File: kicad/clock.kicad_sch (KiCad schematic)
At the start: 15 parts, among them Q2 BC547, SW1 Reset, U18 NE555P, U19 74HC163, X1 25.175 MHz

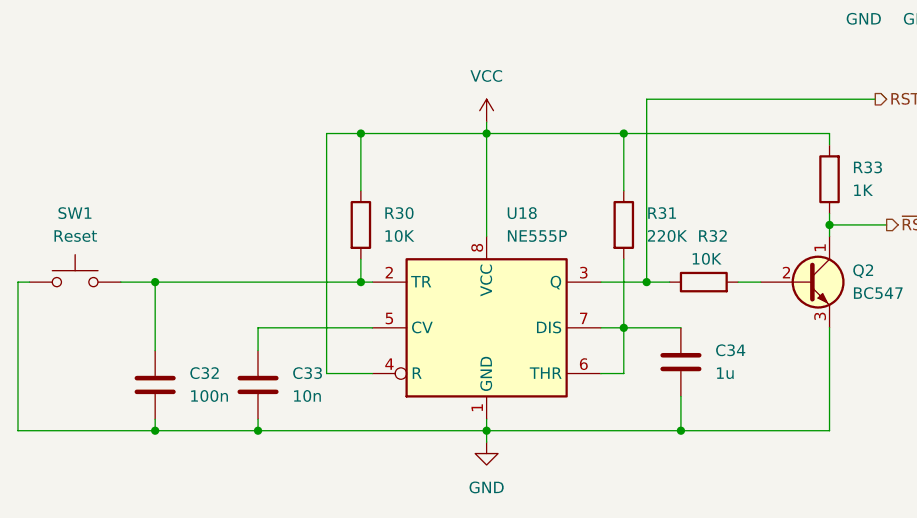
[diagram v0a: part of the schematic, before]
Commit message: HW: Fix unconnected /SOUND net, add /RST header and /DTR power supply
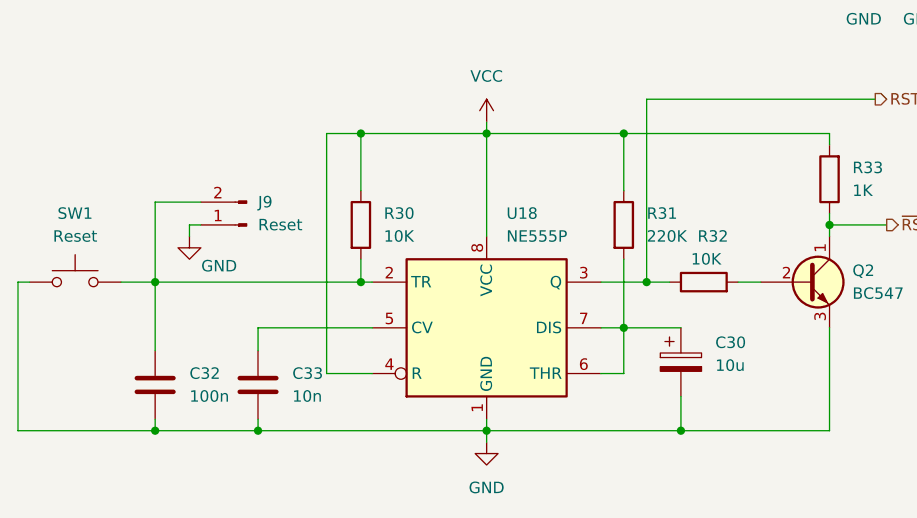
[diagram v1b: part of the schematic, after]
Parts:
- removed C34: 1u, Capacitor_THT:C_Disc_D5.0mm_W2.5mm_P2.50mm, symbol Device:C
- added C30: 10u, Capacitor_THT:CP_Radial_D5.0mm_P2.50mm, symbol Device:C_Polarized
- added J9: Reset, Connector_PinHeader_2.54mm:PinHeader_1x02_P2.54mm_Vertical, symbol Connector:Conn_01x02_Pin
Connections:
- net GND: now also C30.2, J9.1 (Pin_1)
- net at R31.2, U18.6 (THR), U18.7 (DIS): now also C30.1
- net at C32.1, R30.2, SW1.2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: now also J9.2 (Pin_2)
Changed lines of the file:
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@@
+	(wire
+		(pts
+			(xy 101.6 118.11) (xy 102.87 118.11)
+		)
+		(stroke
+			(width 0)
+			(type default)
+		)
+	)
 	(wire
 		(pts
@@
 	(wire
 		(pts
+			(xy 102.87 115.57) (xy 97.79 115.57)
+		)
+		(stroke
+			(width 0)
+			(type default)
+		)
+	)
+	(wire
+		(pts
 			(xy 139.7 40.64) (xy 139.7 49.53)
 		)
@@
 	(wire
 		(pts
+			(xy 101.6 119.38) (xy 101.6 118.11)
+		)
+		(stroke
+			(width 0)
+			(type default)
+		)
+	)
+	(wire
+		(pts
 			(xy 172.72 107.95) (xy 172.72 109.22)
 		)
@@
 		(pts
 			(xy 134.62 142.24) (xy 134.62 140.97)
+		)
+		(stroke
+			(width 0)
+			(type default)
+		)
+	)
+	(wire
+		(pts
+			(xy 97.79 115.57) (xy 97.79 124.46)
 		)
 		(stroke
@@
 	)
 	(symbol
-		(lib_id "Device:C")
-		(at 156.21 133.35 0)
-		(unit 1)
-		(exclude_from_sim no)
-		(in_bom yes)
-		(on_board yes)
-		(dnp no)
-		(fields_autoplaced yes)
-		(property "Reference" "C34"
-			(at 160.02 132.0799 0)
-			(effects
-				(font
-					(size 1.27 1.27)
-				)
-				(justify left)
-			)
-		)
-		(property "Value" "1u"
-			(at 160.02 134.6199 0)
-			(effects
-				(font
-					(size 1.27 1.27)
-				)
-				(justify left)
-			)
-		)
-		(property "Footprint" "Capacitor_THT:C_Disc_D5.0mm_W2.5mm_P2.50mm"
-			(at 157.1752 137.16 0)
-			(effects
-				(font
-					(size 1.27 1.27)
-				)
-				(hide yes)
-			)
-		)
-		(property "Datasheet" "~"
-			(at 156.21 133.35 0)
-			(effects
-				(font
-					(size 1.27 1.27)
-				)
-				(hide yes)
-			)
-		)
-		(property "Description" "Unpolarized capacitor"
-			(at 156.21 133.35 0)
-			(effects
-				(font
-					(size 1.27 1.27)
-				)
-				(hide yes)
-			)
-		)
-		(pin "1"
-		)
-		(pin "2"
-		)
-		(instances
-			(project "zak180"
-				(path "/ca48b56d-33a4-442b-b1b9-aaf2c2c8d68d/7f908845-99aa-4c65-bd74-eb161c1029c6"
-					(reference "C34")
-					(unit 1)
-				)
-			)
-		)
-	)
-	(symbol
 		(lib_id "Switch:SW_Omron_B3FS")
 		(at 88.9 124.46 0)
@@
 	(symbol
 		(lib_id "power:GND")
+		(at 101.6 119.38 0)
+		(unit 1)
+		(exclude_from_sim no)
+		(in_bom yes)
+		(on_board yes)
+		(dnp no)
+		(property "Reference" "#PWR0192"
+			(at 101.6 125.73 0)
+			(effects
+				(font
+					(size 1.27 1.27)
+				)
+				(hide yes)
+			)
+		)
+		(property "Value" "GND"
+			(at 104.902 122.682 0)
+			(effects
+				(font
+					(size 1.27 1.27)
+				)
+			)
+		)
+		(property "Footprint" ""
+			(at 101.6 119.38 0)
+			(effects
+				(font
+					(size 1.27 1.27)
+				)
+				(hide yes)
+			)
+		)
+		(property "Datasheet" ""
+			(at 101.6 119.38 0)
+			(effects
+				(font
+					(size 1.27 1.27)
+				)
+				(hide yes)
+			)
+		)
+		(property "Description" "Power symbol creates a global label with name \"GND\" , ground"
+			(at 101.6 119.38 0)
+			(effects
+				(font
+					(size 1.27 1.27)
+				)
+				(hide yes)
+			)
+		)
+		(pin "1"
+		)
+		(instances
+			(project "zak180"
+				(path "/ca48b56d-33a4-442b-b1b9-aaf2c2c8d68d/7f908845-99aa-4c65-bd74-eb161c1029c6"
+					(reference "#PWR0192")
+					(unit 1)
+				)
+			)
+		)
+	)
+	(symbol
+		(lib_id "power:GND")
 		(at 189.23 90.17 0)
 		(unit 1)
@@
 	)
 	(symbol
+		(lib_id "Device:C_Polarized")
+		(at 156.21 133.35 0)
+		(unit 1)
+		(exclude_from_sim no)
+		(in_bom yes)
+		(on_board yes)
+		(dnp no)
+		(fields_autoplaced yes)
+		(property "Reference" "C30"
+			(at 160.02 131.1909 0)
+			(effects
+				(font
+					(size 1.27 1.27)
+				)
+				(justify left)
+			)
+		)
+		(property "Value" "10u"
+			(at 160.02 133.7309 0)
+			(effects
+				(font
+					(size 1.27 1.27)
+				)
+				(justify left)
+			)
+		)
+		(property "Footprint" "Capacitor_THT:CP_Radial_D5.0mm_P2.50mm"
+			(at 157.1752 137.16 0)
+			(effects
+				(font
+					(size 1.27 1.27)
+				)
+				(hide yes)
+			)
+		)
+		(property "Datasheet" "~"
+			(at 156.21 133.35 0)
+			(effects
+				(font
+					(size 1.27 1.27)
+				)
+				(hide yes)
+			)
+		)
+		(property "Description" "Polarized capacitor"
+			(at 156.21 133.35 0)
+			(effects
+				(font
+					(size 1.27 1.27)
+				)
+				(hide yes)
+			)
+		)
+		(pin "1"
+		)
+		(pin "2"
+		)
+		(instances
+			(project "zak180"
+				(path "/ca48b56d-33a4-442b-b1b9-aaf2c2c8d68d/7f908845-99aa-4c65-bd74-eb161c1029c6"
+					(reference "C30")
+					(unit 1)
+				)
+			)
+		)
+	)
+	(symbol
 		(lib_id "power:VCC")
 		(at 189.23 82.55 0)
@@
 					(unit 1)
 				)
+			)
+		)
+	)
+	(symbol
+		(lib_id "Connector:Conn_01x02_Pin")
+		(at 107.95 118.11 180)
+		(unit 1)
+		(exclude_from_sim no)
+		(in_bom yes)
+		(on_board yes)
+		(dnp no)
+		(fields_autoplaced yes)
+		(property "Reference" "J9"
+			(at 109.22 115.5699 0)
+			(effects
+				(font
+					(size 1.27 1.27)
+				)
+				(justify right)
+			)
+		)
+		(property "Value" "Reset"
+			(at 109.22 118.1099 0)
+			(effects
+				(font
+					(size 1.27 1.27)
+				)
+				(justify right)
+			)
+		)
+		(property "Footprint" "Connector_PinHeader_2.54mm:PinHeader_1x02_P2.54mm_Vertical"
+			(at 107.95 118.11 0)
+			(effects
+				(font
+					(size 1.27 1.27)
+				)
+				(hide yes)
+			)
+		)
+		(property "Datasheet" "~"
+			(at 107.95 118.11 0)
+			(effects
+				(font
+					(size 1.27 1.27)
+				)
+				(hide yes)
+			)
+		)
+		(property "Description" "Generic connector, single row, 01x02, script generated"
+			(at 107.95 118.11 0)
+			(effects
+				(font
+					(size 1.27 1.27)
+				)
+				(hide yes)
+			)
+		)
+		(pin "2"
+		)
+		(pin "1"
+		)
+		(instances
+			(project "zak180"
+				(path "/ca48b56d-33a4-442b-b1b9-aaf2c2c8d68d/7f908845-99aa-4c65-bd74-eb161c1029c6"
+					(reference "J9")
+					(unit 1)
+				)
